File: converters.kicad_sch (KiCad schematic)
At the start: 26 parts, among them J1 USB_C_Receptacle, J2 DC 5V In, Q1 MMBT2222A-TP, SW1 SW_SPDT, U1 AP2112K-1.8, U2 TPS62160DSG

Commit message: Added MAX-M10S GPS, selected antenna and did schematic
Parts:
- R3, R5: value R_US -> 100k
- R4: value R_US -> 312k
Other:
- note added: "DC SUPPLY FOR DEBUG & TESTING"
- note added: "R5 = 100k R4 = 100k((3V3/0.8V) - 1) = 312.5k. USE 312k R3 = 100k, from datasheet"
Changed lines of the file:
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@@
 		)
 	)
+	(text "R5 = 100k\nR4 = 100k((3V3/0.8V) - 1) = 312.5k. USE 312k\nR3 = 100k, from datasheet"
+		(exclude_from_sim no)
+		(at 176.53 84.836 0)
+		(effects
+			(font
+				(size 1.016 1.016)
+				(italic yes)
+			)
+			(justify left)
+		)
+	)
 	(text "LED VF=2V"
 		(exclude_from_sim no)
@@
 		)
 	)
+	(text "DC SUPPLY FOR DEBUG & TESTING"
+		(exclude_from_sim no)
+		(at 64.008 151.892 0)
+		(effects
+			(font
+				(size 1.016 1.016)
+			)
+		)
+	)
 	(text "POWER INDICATION LEDs"
 		(exclude_from_sim no)
@@
 			)
 		)
-		(property "Value" "R_US"
+		(property "Value" "100k"
 			(at 241.3 69.8499 0)
 			(show_name no)
@@
 			)
 		)
-		(property "Value" "R_US"
+		(property "Value" "100k"
 			(at 222.25 59.944 90)
 			(show_name no)
@@
 			)
 		)
-		(property "Value" "R_US"
+		(property "Value" "312k"
 			(at 241.3 60.9599 0)
 			(show_name no)

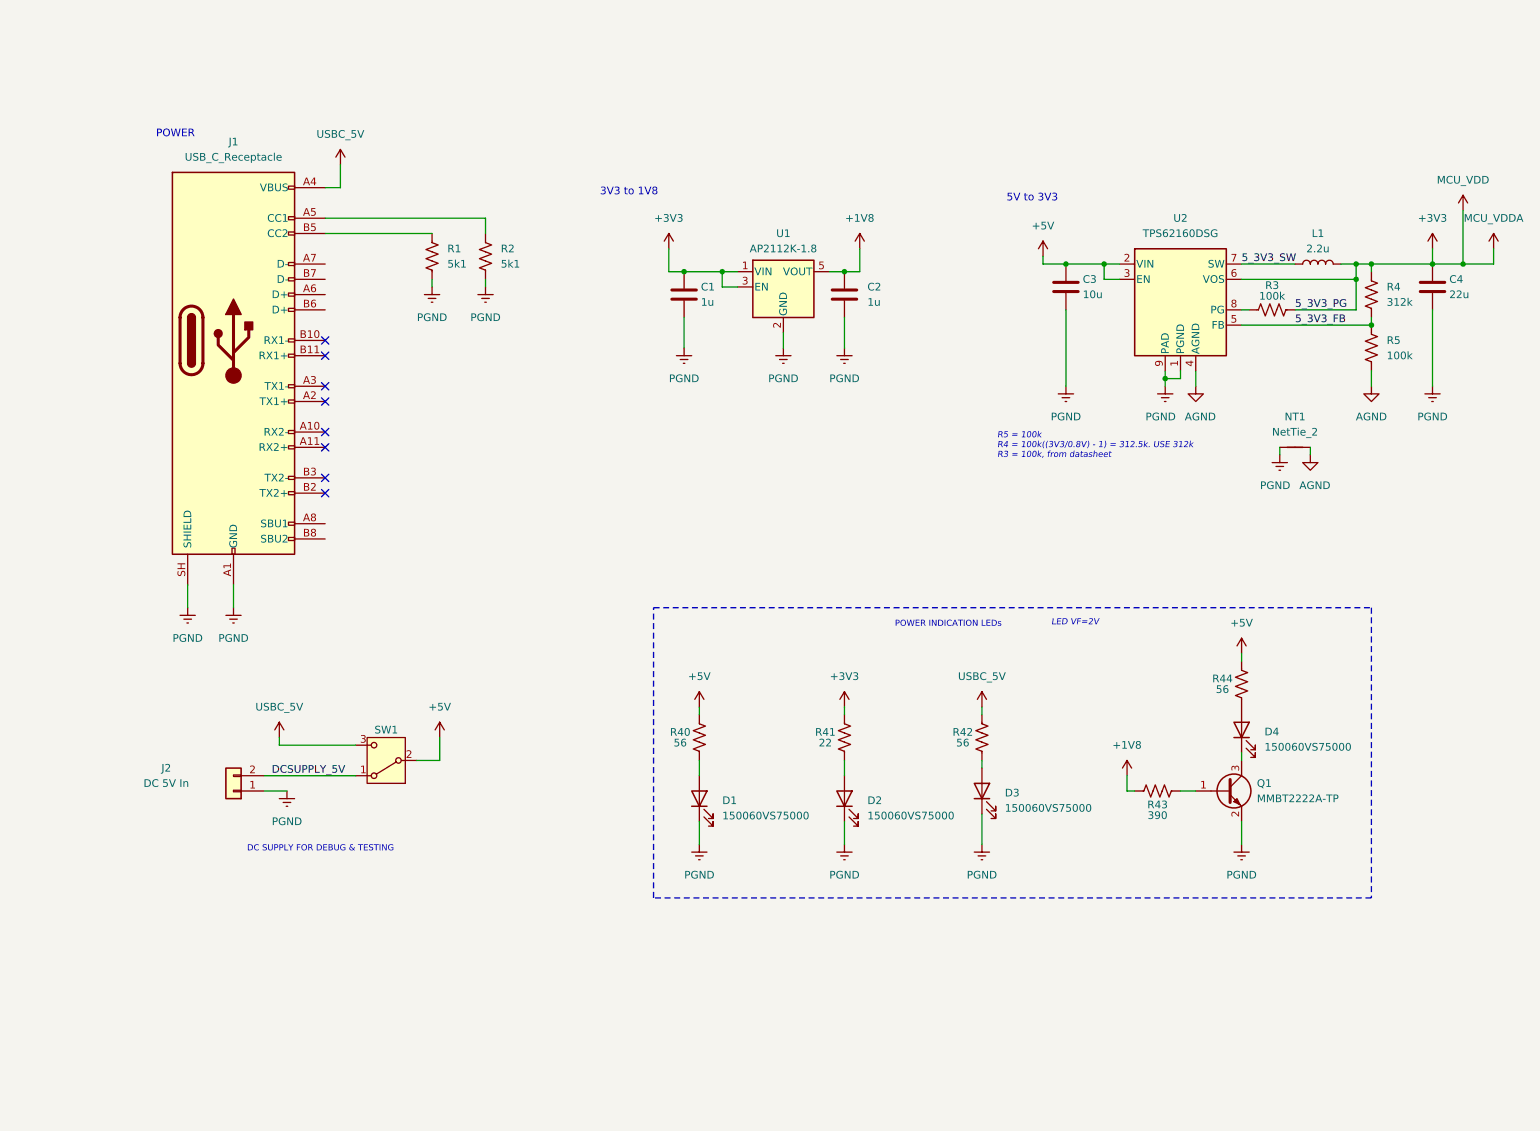
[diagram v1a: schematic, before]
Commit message: Schematics complete; Starting layout. Removed 2 thermistors, not necessary. Going to update website once layout starts
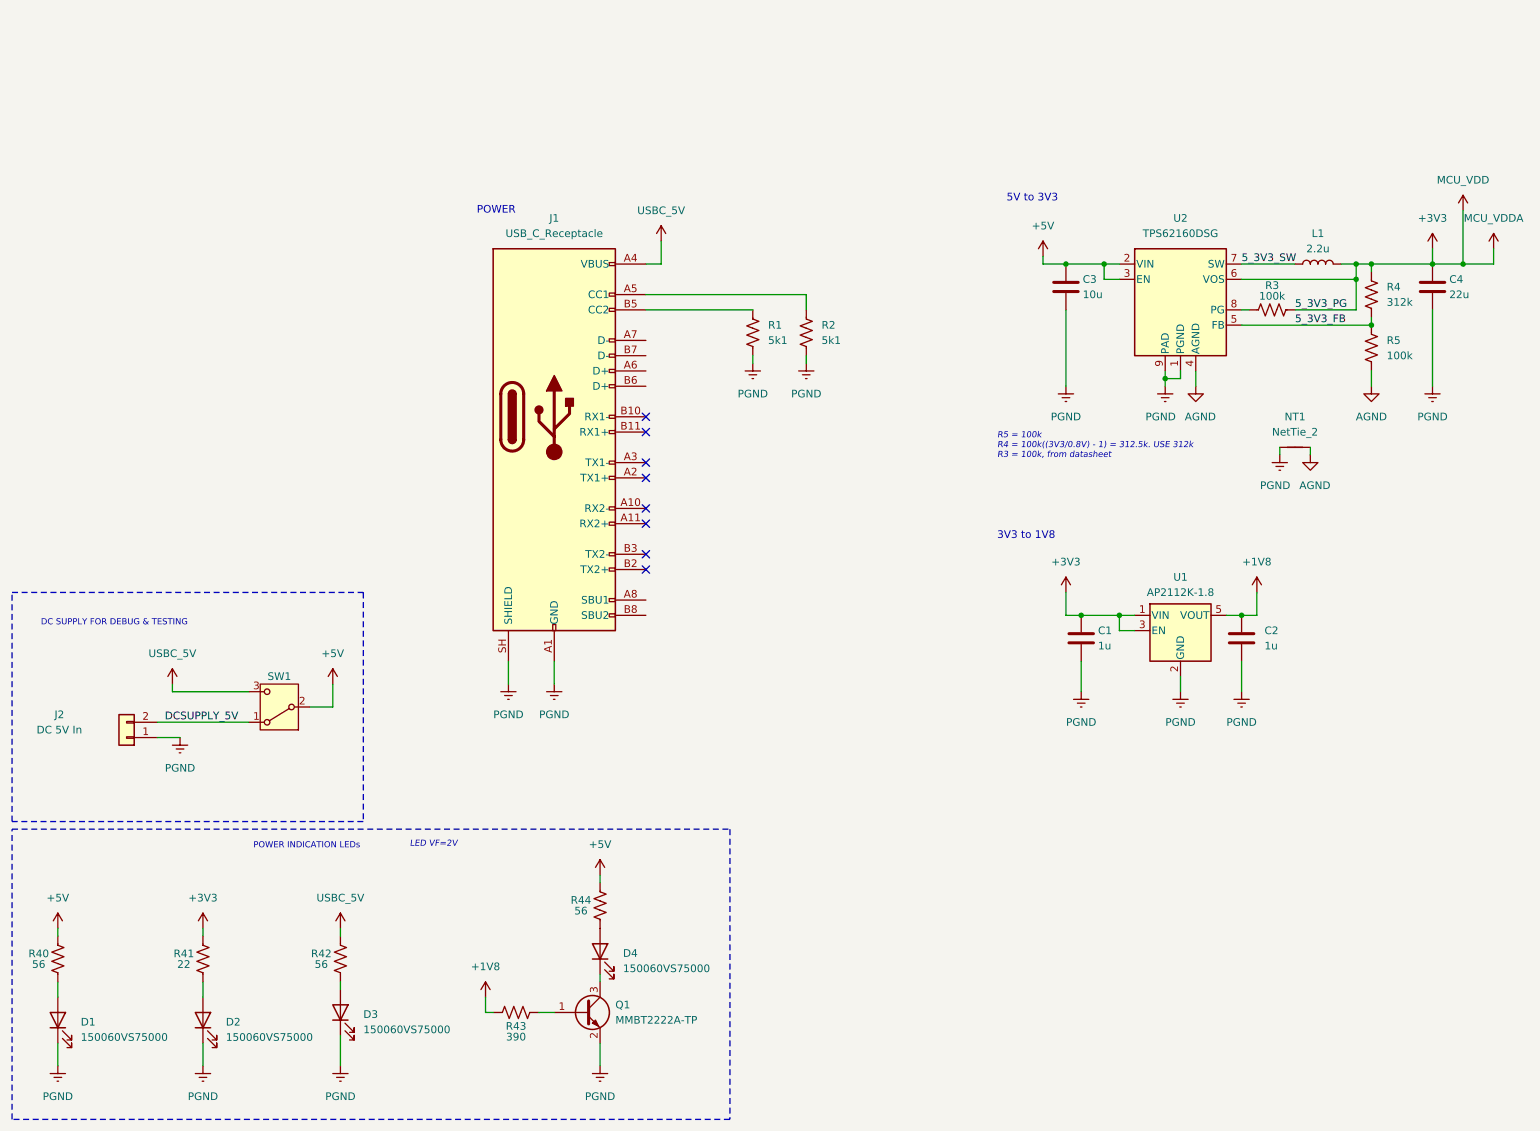
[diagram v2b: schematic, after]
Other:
- moved on the sheet: C1, C2, D1, D2, D3, D4, J1, J2, Q1, R1, R2, R40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

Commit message: Final schematic and initial layout
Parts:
- removed D3: 150060VS75000, LED_SMD:LED_0603_1608Metric, symbol Device:LED
- removed NT1: NetTie_2, NetTie:NetTie-2_SMD_Pad0.5mm, symbol Device:NetTie_2
- removed R42: 56, Resistor_SMD:R_0603_1608Metric, symbol Device:R_US
- removed SW1: SW_SPDT, Telem_fp:CL-SB-12B-02T_NDC, symbol Switch:SW_SPDT
- C1, C2, C3, C4: footprint Capacitor_SMD:C_0805_2012Metric_Pad1.18x1.45mm_HandSolder -> Capacitor_SMD:C_0805_2012Metric
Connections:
- net DCSUPPLY_5V is gone; now on net +5V: J2.2 (Pin_2)
- net USBC_5V is gone; now on net +5V: J1.A4 (VBUS), J1.A9 (VBUS), J1.B4 (VBUS), J1.B9 (VBUS)
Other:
- moved on the sheet: D1, D2, D4, Q1, R40, R41, R43, R44

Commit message: Finished initial signal layout
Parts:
- J2: footprint Connector_Wire:SolderWire-0.5sqmm_1x02_P4.6mm_D0.9mm_OD2.1mm -> Connector_PinHeader_2.00mm:PinHeader_1x02_P2.00mm_Vertical
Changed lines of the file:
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@@
 			)
 		)
-		(property "Footprint" "Connector_Wire:SolderWire-0.5sqmm_1x02_P4.6mm_D0.9mm_OD2.1mm"
+		(property "Footprint" "Connector_PinHeader_2.00mm:PinHeader_1x02_P2.00mm_Vertical"
 			(at 31.75 133.35 0)
 			(hide yes)

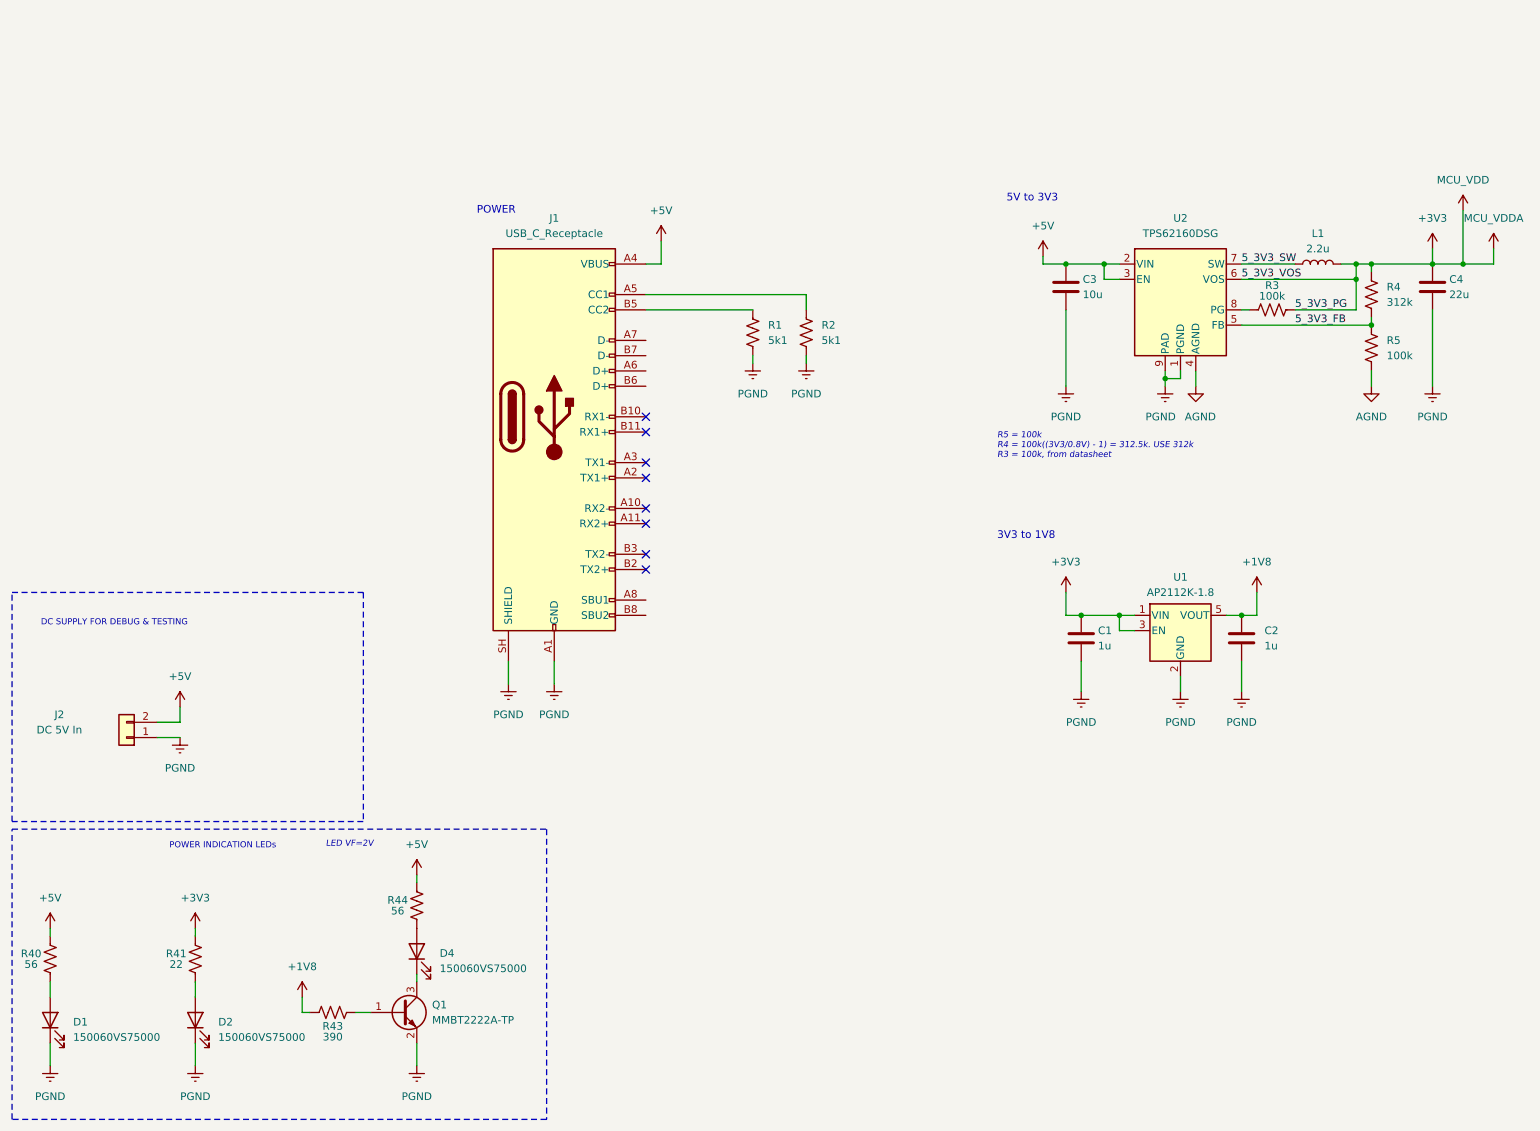
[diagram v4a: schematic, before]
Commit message: Updated schematics to add SD, will finish SD next and redo layout
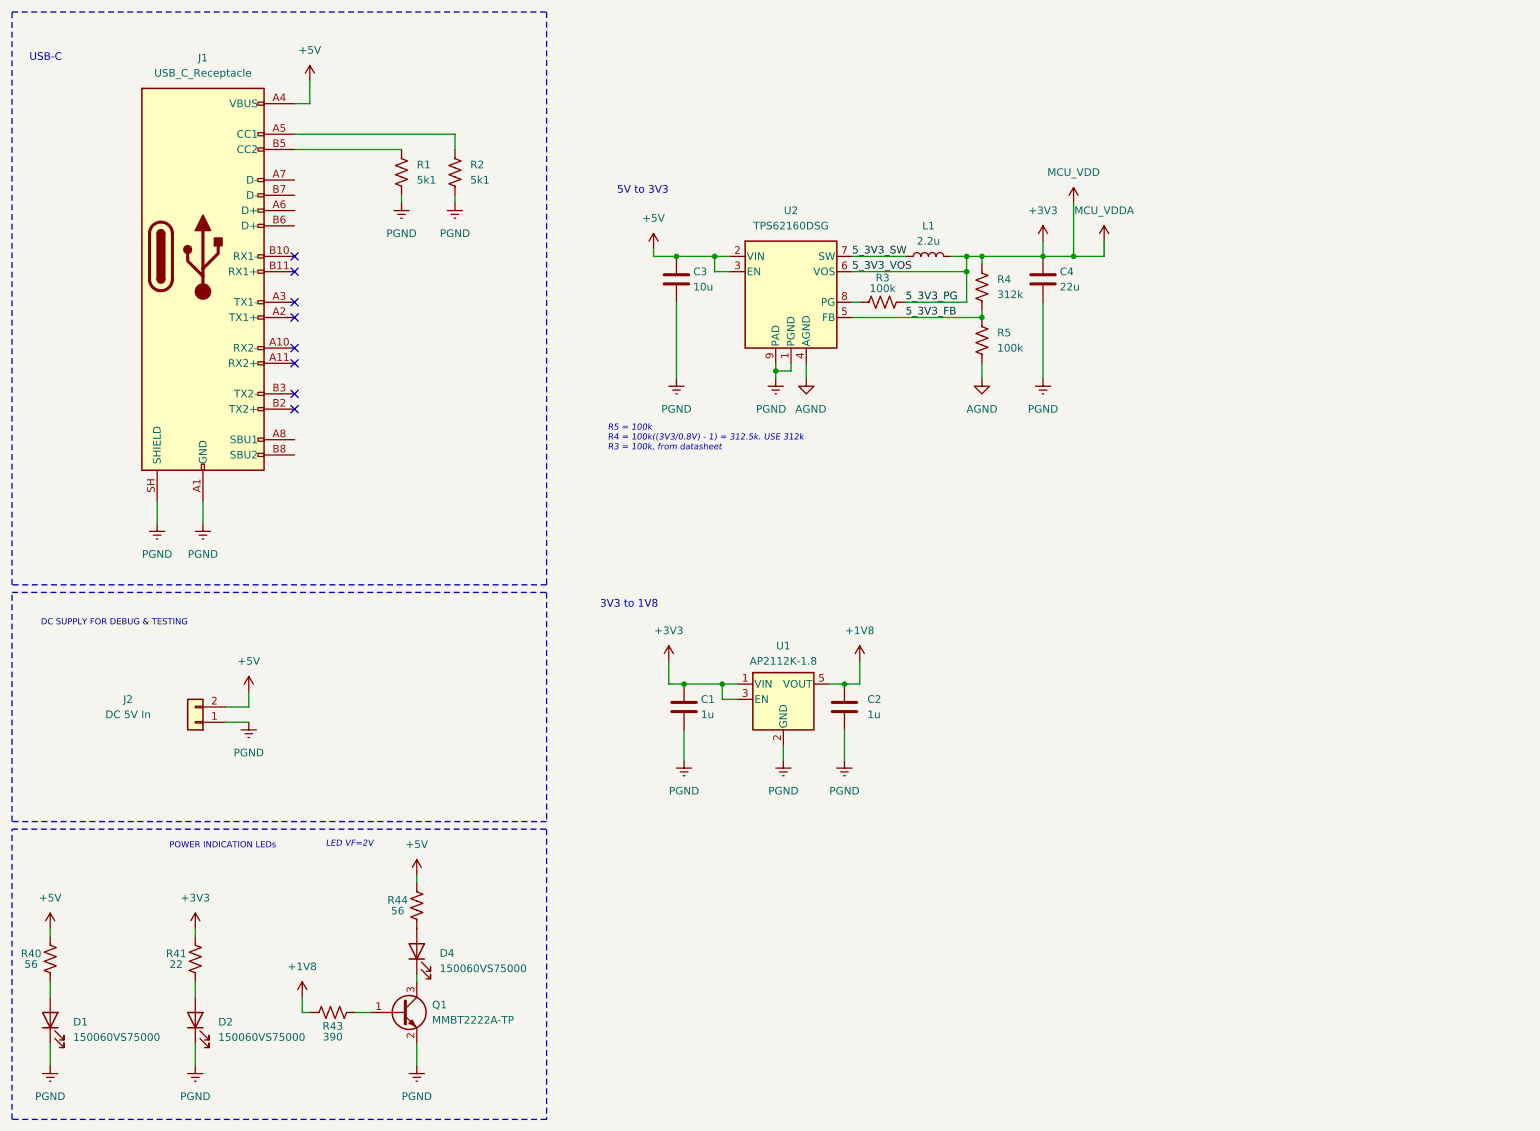
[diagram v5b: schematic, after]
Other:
- note added: "USB-C"
- note removed: "POWER"
- moved on the sheet: C1, C2, C3, C4, J1, J2, L1, R1, R2, R3, R4, R5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

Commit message: Updated schematics for rev2
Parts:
- added U9: USBLC6-2P6, Package_TO_SOT_SMD:SOT-666, symbol Power_Protection:USBLC6-2P6
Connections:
- net +5V: now also U9.5 (VBUS)
- net PGND: now also U9.2 (GND)
- net USB_D+: now reaches J1.A6 (D+)
- net USB_D+: now also J1.B6 (D+), U9.1 (I/O1)
- net USB_D-: now reaches J1.A7 (D-)
- net USB_D-: now also J1.B7 (D-), U9.3 (I/O2)
- net 5_3V3_FB renamed 5_+3V3_FB
- net 5_3V3_SW renamed 5_+3V3_SW
- new net USB_DN: U9.4 (I/O2)
- new net USB_DP: U9.6 (I/O1)
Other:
- note added: "+3V3 to 1V8"
- note added: "5V to +3V3"
- note added: "ESD Protection"
- note added: "R5 = 100k R4 = 100k((+3V3/0.8V) - 1) = 312.5k. USE 312k R3 = 100k, from datasheet"
- note removed: "3V3 to 1V8"
- note removed: "5V to 3V3"
- note removed: "R5 = 100k R4 = 100k((3V3/0.8V) - 1) = 312.5k. USE 312k R3 = 100k, from datasheet"
- moved on the sheet: J1, J2, R1, R2
